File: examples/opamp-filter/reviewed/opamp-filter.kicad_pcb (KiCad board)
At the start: 2 copper layers, 58 x 42 mm, 22 parts, among them J1 IN, J2 5V, J3 OUT, U1 MCP6001R, U2 MCP6001R

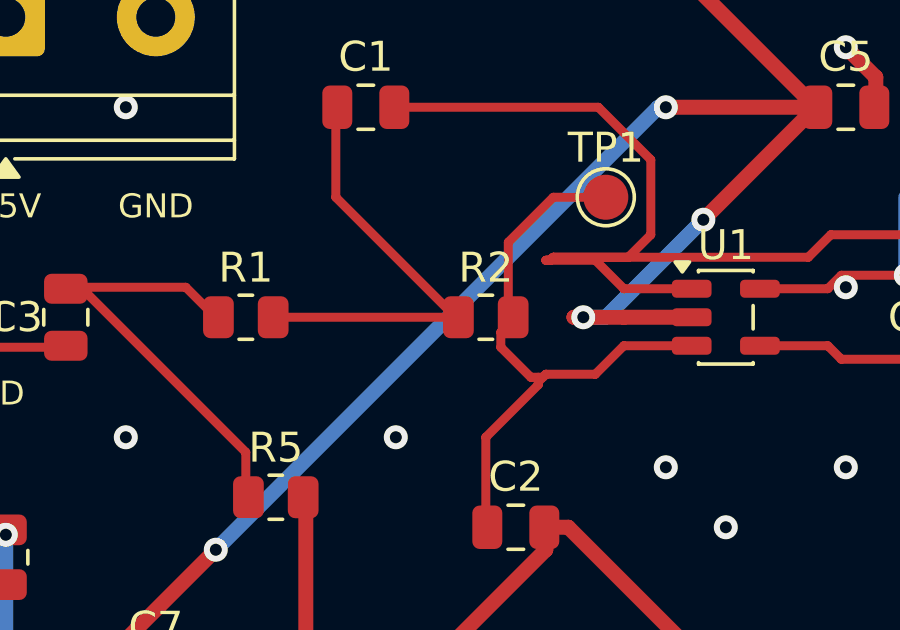
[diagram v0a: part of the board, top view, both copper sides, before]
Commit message: Take out the copper a run lays down and walks back along
Joining two routes at a shared end left the polyline going out past the
join and straight back to it. That is the zero-degree corner
route.acute_angle was reporting on the opamp and the motor board, and on
the plot it reads as a spur with no explanation, because it is one - the
overshoot carries no current.

Only an exact reversal that stops short of where it set out from, and
never a corner another track ends on: that is a join, however it looks.
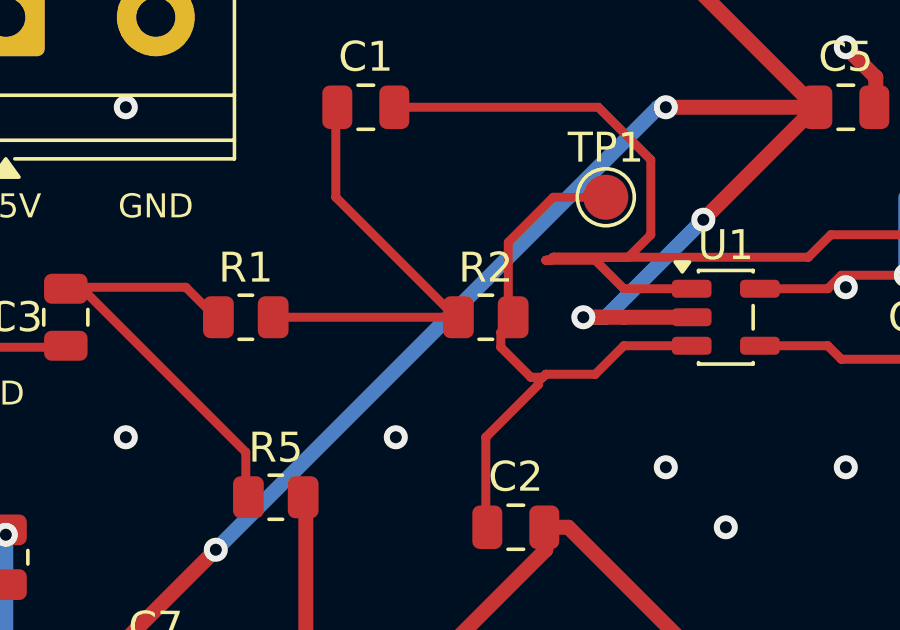
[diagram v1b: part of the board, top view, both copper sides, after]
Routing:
- net +5V: track 97.5 -> 96.9 mm
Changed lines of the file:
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@@
 	(segment (start 128.65 75.1) (end 127.0 75.1) (width 0.3) (layer "F.Cu") (net 7))
 	(segment (start 131.8625 77.0) (end 129.6 77.0) (width 0.5) (layer "F.Cu") (net 2))
-	(segment (start 129.6 77.0) (end 127.938 77.0) (width 0.5) (layer "F.Cu") (net 2))
-	(segment (start 127.938 77.0) (end 128.25 77.0) (width 0.5) (layer "F.Cu") (net 2))
+	(segment (start 129.6 77.0) (end 128.25 77.0) (width 0.5) (layer "F.Cu") (net 2))
 	(segment (start 131.8625 77.95) (end 129.6 77.95) (width 0.3) (layer "F.Cu") (net 3))
 	(segment (start 129.6 77.95) (end 128.65 78.9) (width 0.3) (layer "F.Cu") (net 3))
@@
 	(segment (start 117.0 82.75) (end 117.0 82.9125) (width 0.3) (layer "F.Cu") (net 5))
 	(segment (start 117.0 82.9125) (end 117.0875 83.0) (width 0.3) (layer "F.Cu") (net 5))
-	(segment (start 117.9125 77.0) (end 124.0875 77.0) (width 0.3) (layer "F.Cu") (net 10))
-	(segment (start 124.0875 77.0) (end 124.0 77.0) (width 0.3) (layer "F.Cu") (net 10))
-	(segment (start 124.0 77.0) (end 123.75 76.75) (width 0.3) (layer "F.Cu") (net 10))
+	(segment (start 117.9125 77.0) (end 123.823 77.0) (width 0.3) (layer "F.Cu") (net 10))
+	(segment (start 123.823 77.0) (end 123.823 76.927) (width 0.3) (layer "F.Cu") (net 10))
+	(segment (start 123.823 76.927) (end 123.875 76.875) (width 0.3) (layer "F.Cu") (net 10))
+	(segment (start 123.875 76.875) (end 123.75 76.75) (width 0.3) (layer "F.Cu") (net 10))
 	(segment (start 123.75 76.75) (end 120.0 73.0) (width 0.3) (layer "F.Cu") (net 10))
 	(segment (start 120.0 73.0) (end 120.0 70.25) (width 0.3) (layer "F.Cu") (net 10))
